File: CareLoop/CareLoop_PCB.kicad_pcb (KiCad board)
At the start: 2 copper layers, 38 parts, among them J1 Conn_01x02_Pin, J1_DEBUG1 Conn_01x04_Pin, J2 USB_B_Micro, J3 Conn_01x02_Pin, SW1 SW_Push, U1 nRF52840-QFXX, U2 MAX30102, U3 MPU-6050, U4 MCP1700x-330xxMB, U5 TP4056-42-ESOP8, Y1 32Mhz

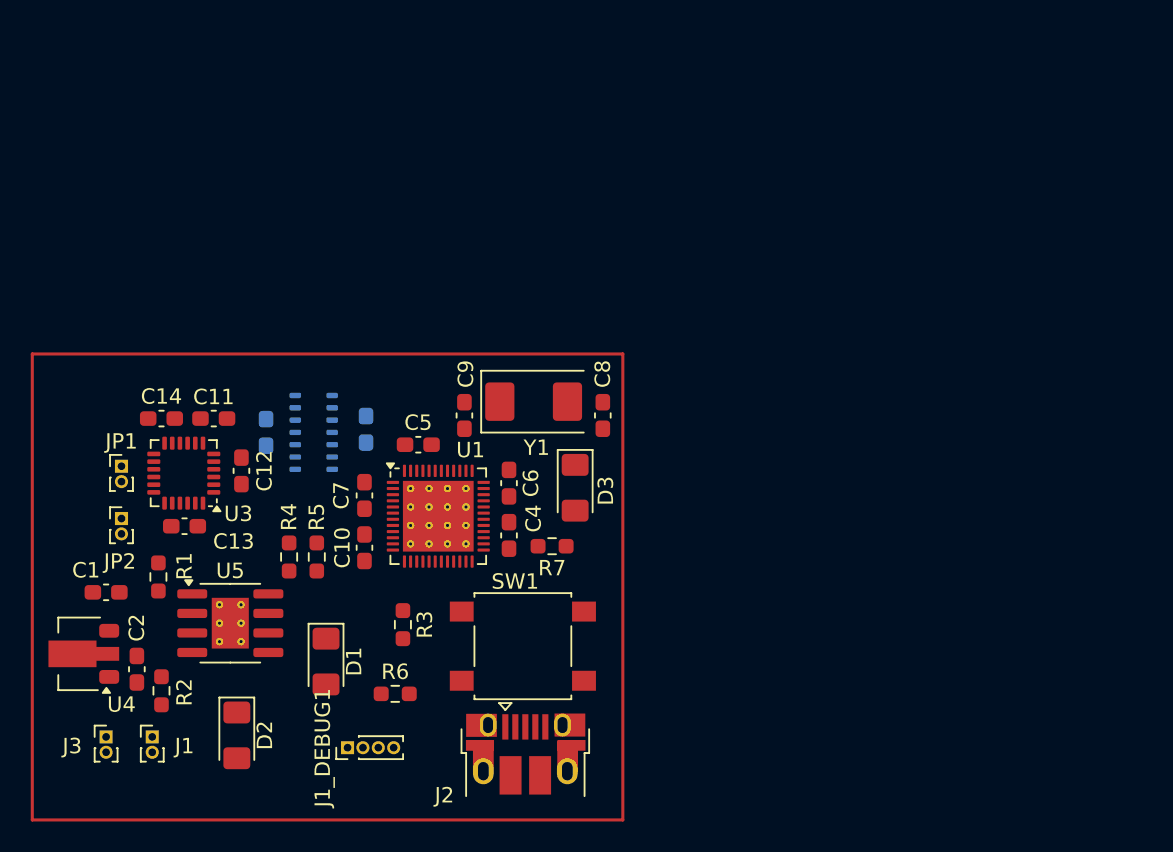
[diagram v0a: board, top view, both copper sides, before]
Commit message: WP: Placement PCB Parts done
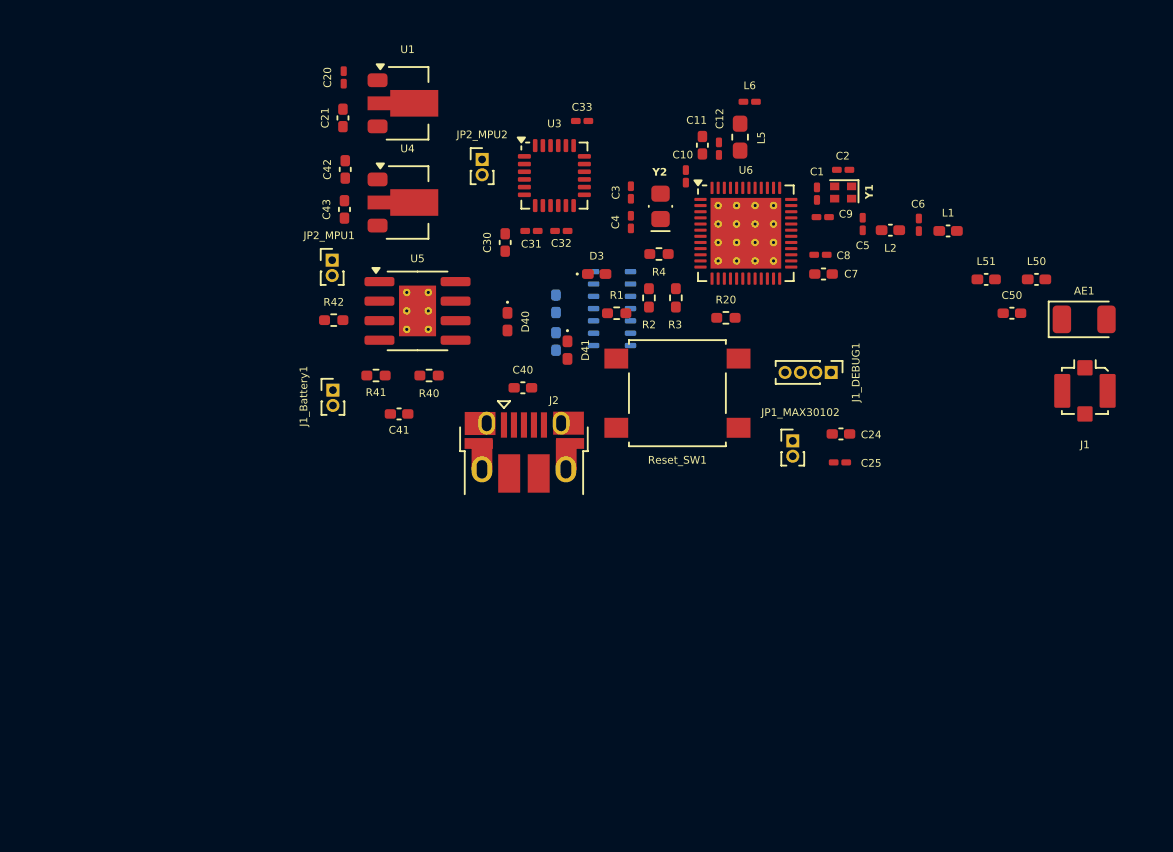
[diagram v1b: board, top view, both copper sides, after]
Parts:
- removed C13: 2.2n, Capacitor_SMD:C_0603_1608Metric_Pad1.08x0.95mm_HandSolder
- removed C14, C15: 100n, Capacitor_SMD:C_0603_1608Metric_Pad1.08x0.95mm_HandSolder
- removed D1, D2: LED, LED_SMD:LED_1206_3216Metric_Pad1.42x1.75mm_HandSolder
- removed J3: Conn_01x02_Pin, Connector_PinHeader_1.00mm:PinHeader_1x02_P1.00mm_Vertical
- removed JP1, JP2: Jumper_2_Bridged, Connector_PinHeader_1.00mm:PinHeader_1x02_P1.00mm_Vertical
- removed R5: 4k7, Resistor_SMD:R_0603_1608Metric_Pad0.98x0.95mm_HandSolder
- removed R6: 1k, Resistor_SMD:R_0603_1608Metric_Pad0.98x0.95mm_HandSolder
- removed R7: 325, Resistor_SMD:R_0603_1608Metric_Pad0.98x0.95mm_HandSolder
- removed SW1: SW_Push, Button_Switch_SMD:SW_SPST_B3S-1000
- added AE1: Antenna_Chip, RF_Antenna:Johanson_2450AT18x100, F.Cu at (192.8, 75.2)
- added C20: 100n, Capacitor_SMD:C_0201_0603Metric_Pad0.64x0.40mm_HandSolder, F.Cu at (144.7, 59.4)
- added C21: 4.7u, Capacitor_SMD:C_0402_1005Metric_Pad0.74x0.62mm_HandSolder, F.Cu at (144.6, 62.0)
- added C22: 1u, Capacitor_SMD:C_0402_1005Metric_Pad0.74x0.62mm_HandSolder, B.Cu at (158.5, 76.6)
- added C23: 4.7u, Capacitor_SMD:C_0402_1005Metric_Pad0.74x0.62mm_HandSolder, B.Cu at (158.5, 74.1)
- added C24: 10u, Capacitor_SMD:C_0402_1005Metric_Pad0.74x0.62mm_HandSolder, F.Cu at (177.0, 82.6)
- added C25: 100n, Capacitor_SMD:C_0201_0603Metric_Pad0.64x0.40mm_HandSolder, F.Cu at (176.9, 84.5)
- added C30: 10n, Capacitor_SMD:C_0402_1005Metric_Pad0.74x0.62mm_HandSolder, F.Cu at (155.2, 70.2)
- added C31: 100n, Capacitor_SMD:C_0201_0603Metric_Pad0.64x0.40mm_HandSolder, F.Cu at (156.9, 69.4)
- added C32: 100n, Capacitor_SMD:C_0201_0603Metric_Pad0.64x0.40mm_HandSolder, F.Cu at (158.8, 69.4)
- added C33: 2.2n, Capacitor_SMD:C_0201_0603Metric_Pad0.64x0.40mm_HandSolder, F.Cu at (160.2, 62.2)
- added C40: 1u, Capacitor_SMD:C_0402_1005Metric_Pad0.74x0.62mm_HandSolder, F.Cu at (156.3, 79.6)
- added C41: 10u, Capacitor_SMD:C_0402_1005Metric_Pad0.74x0.62mm_HandSolder, F.Cu at (148.2, 81.3)
- added C42: 1u, Capacitor_SMD:C_0402_1005Metric_Pad0.74x0.62mm_HandSolder, F.Cu at (144.8, 65.4)
- added C43: 1u, Capacitor_SMD:C_0402_1005Metric_Pad0.74x0.62mm_HandSolder, F.Cu at (144.7, 68.0)
- added C50: C_Small, Capacitor_SMD:C_0402_1005Metric_Pad0.74x0.62mm_HandSolder, F.Cu at (188.1, 74.8)
- added D40: LED, LED_SMD:LED_0402_1005Metric_Pad0.77x0.64mm_HandSolder, F.Cu at (155.3, 75.3)
- added D41: LED, LED_SMD:LED_0402_1005Metric_Pad0.77x0.64mm_HandSolder, F.Cu at (159.2, 77.2)
- added J1_Battery1: Conn_01x02_Pin, Connector_PinHeader_1.00mm:PinHeader_1x02_P1.00mm_Vertical, F.Cu at (143.9, 79.8)
- added JP1_MAX30102: Jumper_2_Bridged, Connector_PinHeader_1.00mm:PinHeader_1x02_P1.00mm_Vertical, F.Cu at (173.8, 83.0)
- added JP2_MPU1: Jumper_2_Bridged, Connector_PinHeader_1.00mm:PinHeader_1x02_P1.00mm_Vertical, F.Cu at (143.9, 71.3)
- added JP2_MPU2: Jumper_2_Bridged, Connector_PinHeader_1.00mm:PinHeader_1x02_P1.00mm_Vertical, F.Cu at (153.7, 64.8)
- added L1: 2.2n, Inductor_SMD:L_0402_1005Metric_Pad0.77x0.64mm_HandSolder, F.Cu at (183.9, 69.4)
- added L2: 4.7n, Inductor_SMD:L_0402_1005Metric_Pad0.77x0.64mm_HandSolder, F.Cu at (180.2, 69.3)
- added L5: 10u, Inductor_SMD:L_0603_1608Metric_Pad1.05x0.95mm_HandSolder, F.Cu at (170.4, 63.3)
- added L50: L_Small, Inductor_SMD:L_0402_1005Metric_Pad0.77x0.64mm_HandSolder, F.Cu at (189.7, 72.5)
- added L51: L_Small, Inductor_SMD:L_0402_1005Metric_Pad0.77x0.64mm_HandSolder, F.Cu at (186.4, 72.5)
- added L6: 15n, Inductor_SMD:L_0201_0603Metric_Pad0.64x0.40mm_HandSolder, F.Cu at (171.1, 61.0)
- added R20: 10k, Resistor_SMD:R_0402_1005Metric_Pad0.72x0.64mm_HandSolder, F.Cu at (169.5, 75.0)
- added R40: 1k, Resistor_SMD:R_0402_1005Metric_Pad0.72x0.64mm_HandSolder, F.Cu at (150.2, 78.8)
- added R41: 1k, Resistor_SMD:R_0402_1005Metric_Pad0.72x0.64mm_HandSolder, F.Cu at (146.8, 78.8)
- added R42: 20k, Resistor_SMD:R_0402_1005Metric_Pad0.72x0.64mm_HandSolder, F.Cu at (144.0, 75.2)
- added Reset_SW1: SW_Push, Button_Switch_SMD:SW_SPST_B3S-1000, F.Cu at (166.3, 80.0)
- added U6: nRF52840-QFXX, Package_DFN_QFN:QFN-48-1EP_6x6mm_P0.4mm_EP4.6x4.6mm_ThermalVias, F.Cu at (170.8, 69.5)
- added Y2: 32.768kHz, Crystal:Crystal_SMD_MicroCrystal_CM9V-T1A-2Pin_1.6x1.0mm_HandSoldering, F.Cu at (165.2, 67.8)
- C1, C2: value 1u -> 12p; footprint Capacitor_SMD:C_0603_1608Metric_Pad1.08x0.95mm_HandSolder -> Capacitor_SMD:C_0201_0603Metric_Pad0.64x0.40mm_HandSolder
- C10: value 100n -> 100p; footprint Capacitor_SMD:C_0603_1608Metric_Pad1.08x0.95mm_HandSolder -> Capacitor_SMD:C_0201_0603Metric_Pad0.64x0.40mm_HandSolder
- C11: value 10n -> 1u; footprint Capacitor_SMD:C_0603_1608Metric_Pad1.08x0.95mm_HandSolder -> Capacitor_SMD:C_0402_1005Metric_Pad0.74x0.62mm_HandSolder
- C12: footprint Capacitor_SMD:C_0603_1608Metric_Pad1.08x0.95mm_HandSolder -> Capacitor_SMD:C_0201_0603Metric_Pad0.64x0.40mm_HandSolder
- C3: value 1u -> 12p; footprint Capacitor_SMD:C_0603_1608Metric_Pad1.08x0.95mm_HandSolder -> Capacitor_SMD:C_0201_0603Metric_Pad0.64x0.40mm_HandSolder; moved to F.Cu
- C4: value 4.7u -> 12p; footprint Capacitor_SMD:C_0603_1608Metric_Pad1.08x0.95mm_HandSolder -> Capacitor_SMD:C_0201_0603Metric_Pad0.64x0.40mm_HandSolder
- C5: value 1.0u -> 1p; footprint Capacitor_SMD:C_0603_1608Metric_Pad1.08x0.95mm_HandSolder -> Capacitor_SMD:C_0201_0603Metric_Pad0.64x0.40mm_HandSolder
- C6: value 1.0u -> 1.2p; footprint Capacitor_SMD:C_0603_1608Metric_Pad1.08x0.95mm_HandSolder -> Capacitor_SMD:C_0201_0603Metric_Pad0.64x0.40mm_HandSolder
- C7: value 1.0u -> 1u; footprint Capacitor_SMD:C_0603_1608Metric_Pad1.08x0.95mm_HandSolder -> Capacitor_SMD:C_0402_1005Metric_Pad0.74x0.62mm_HandSolder
- C8: value 12p -> 47n; footprint Capacitor_SMD:C_0603_1608Metric_Pad1.08x0.95mm_HandSolder -> Capacitor_SMD:C_0201_0603Metric_Pad0.64x0.40mm_HandSolder
- C9: value 12p -> 100p; footprint Capacitor_SMD:C_0603_1608Metric_Pad1.08x0.95mm_HandSolder -> Capacitor_SMD:C_0201_0603Metric_Pad0.64x0.40mm_HandSolder
- D3: value LED -> LED_Small; footprint LED_SMD:LED_1206_3216Metric_Pad1.42x1.75mm_HandSolder -> LED_SMD:LED_0402_1005Metric_Pad0.77x0.64mm_HandSolder
- J1: value Conn_01x02_Pin -> Conn_Coaxial_Small; footprint Connector_PinHeader_1.00mm:PinHeader_1x02_P1.00mm_Vertical -> Connector_Coaxial:U.FL_Molex_MCRF_73412-0110_Vertical
- R1: value 20k -> 10k; footprint Resistor_SMD:R_0603_1608Metric_Pad0.98x0.95mm_HandSolder -> Resistor_SMD:R_0402_1005Metric_Pad0.72x0.64mm_HandSolder
- R2: value 1k -> 4k7; footprint Resistor_SMD:R_0603_1608Metric_Pad0.98x0.95mm_HandSolder -> Resistor_SMD:R_0402_1005Metric_Pad0.72x0.64mm_HandSolder
- R3: value 10k -> 4k7; footprint Resistor_SMD:R_0603_1608Metric_Pad0.98x0.95mm_HandSolder -> Resistor_SMD:R_0402_1005Metric_Pad0.72x0.64mm_HandSolder
- R4: value 4k7 -> 300; footprint Resistor_SMD:R_0603_1608Metric_Pad0.98x0.95mm_HandSolder -> Resistor_SMD:R_0402_1005Metric_Pad0.72x0.64mm_HandSolder
- U1: value nRF52840-QFXX -> MCP1700x-180xxMB; footprint Package_DFN_QFN:QFN-48-1EP_6x6mm_P0.4mm_EP4.6x4.6mm_ThermalVias -> Package_TO_SOT_SMD:SOT-89-3
- Y1: value 32Mhz -> 32MHz; footprint Crystal:Crystal_SMD_0603-2Pin_6.0x3.5mm -> Oscillator:Oscillator_SMD_Abracon_ASCO-4Pin_1.6x1.2mm
- moved J1 64.7 mm to (192.8, 79.8)
- moved C2 56.2 mm to (177.1, 65.4), turned to 0 degrees
- moved C1 53.0 mm to (175.4, 67.0), turned to 90 degrees
- moved R2 40.7 mm to (164.5, 73.8)
- moved J1_DEBUG1 39.8 mm to (176.3, 78.6), turned to -90 degrees
- moved C12 37.5 mm to (169.1, 64.0), turned to -90 degrees
- moved C11 36.4 mm to (168.0, 63.8), turned to -90 degrees
- moved U4 36.3 mm to (148.8, 67.5), turned to 0 degrees
- moved R1 34.4 mm to (162.4, 74.8), turned to 0 degrees
- moved C7 33.1 mm to (175.8, 72.2), turned to 0 degrees
- moved C5 32.3 mm to (178.4, 69.0), turned to 90 degrees
- moved C10 31.9 mm to (166.9, 65.8), turned to -90 degrees
- moved C6 31.5 mm to (182.1, 69.0), turned to 90 degrees
- moved R4 31.1 mm to (165.2, 70.9), turned to 180 degrees
- moved U3 30.9 mm to (158.3, 65.8), turned to 0 degrees
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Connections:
- C1 pad 1: /Battery/Vout -> GND
- C1 pad 2: Net-(J1-Pin_1) -> Net-(U6-XC1)
- C10 pad 1: /Battery/Vout -> GND
- C10 pad 2: GND -> Net-(U6-DEC1)
- C11 pad 1: Net-(U3-VLOGIC) -> GND
- C11 pad 2: GND -> /Battery/VCC
- C12 pad 1: Net-(U3-VDD) -> GND
- C12 pad 2: GND -> /Battery/VCC
- C2 pad 1: Net-(U4-VI) -> GND
- C2 pad 2: Net-(J1-Pin_1) -> Net-(U6-XC2)
- C3 pad 1: Net-(JP1-A) -> Net-(U6-P0.00)
- C4 pad 1: Net-(U1-DEC6) -> Net-(U6-P0.01)
- C5 pad 1: Net-(U1-DEC4) -> Net-(U6-ANT)
- C6 pad 1: Net-(U1-DEC3) -> Net-(C6-Pad1)
- C7 pad 1: Net-(U1-DEC1) -> Net-(U6-DEC4)
- C8 pad 1: GND -> Net-(U6-DEC4)
- C8 pad 2: Net-(U1-XC1) -> GND
- C9 pad 2: Net-(U1-XC2) -> Net-(U6-DEC3)
- J1 pad 1: Net-(J1-Pin_1) -> /Antenna/ANT
- J1 pad 2: Net-(J1-Pin_2) -> Net-(J1-Ext)
- J1_DEBUG1 pad 4: /Battery/Vout -> /Battery/VCC
- R1 pad 1: Net-(U5-PROG) -> Net-(U6-~{RESET})
- R1 pad 2: GND -> /Battery/VCC
- R2 pad 1: Net-(D2-A) -> /Battery/VCC
- R2 pad 2: Net-(J2-VBUS) -> /MAX30102/SDA
- R3 pad 1: Net-(U1-~{RESET}) -> /Battery/VCC
- R3 pad 2: /Battery/Vout -> /MAX30102/SCL
- R4 pad 1: /Battery/Vout -> Net-(U6-P0.07)
- R4 pad 2: /MAX30102/SDA -> Net-(D3-A)
- U1 pad 1: Net-(U1-DEC1) -> GND
- U1 pad 2: /MCU/INT_MPU -> Net-(JP1_MAX30102-A)
- U1 pad 3: unconnected-(U1-P0.01-Pad3) -> Net-(U1-VO)
- U2 pad 10: Net-(JP1-A) -> Net-(JP1_MAX30102-A)
- U2 pad 11: Net-(JP1-A) -> Net-(U1-VO)
- U2 pad 13: unconnected-(U2-~{INT}-Pad13) -> /MAX30102/MAX_INT
- U2 pad 9: Net-(JP1-A) -> Net-(JP1_MAX30102-A)
- U3 pad 13: Net-(U3-VDD) -> Net-(JP2_MPU2-A)
- U3 pad 8: Net-(U3-VLOGIC) -> Net-(JP2_MPU2-A)
- U4 pad 1: Net-(J1-Pin_1) -> GND
- U4 pad 2: Net-(U4-VI) -> Net-(JP2_MPU1-A)
- U4 pad 3: /Battery/Vout -> /Battery/VCC
- U5 pad 5: Net-(J1-Pin_2) -> Net-(J1_Battery1-Pin_2)
- U5 pad 8: GND -> Net-(J2-VBUS)
- Y1 pad 1: Net-(U1-XC2) -> Net-(U6-XC2)
- Y1 pad 2: Net-(U1-XC1) -> (no net)

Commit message: WP: updatet version with routing
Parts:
- added C26: 100p, Capacitor_SMD:C_0201_0603Metric_Pad0.64x0.40mm_HandSolder, F.Cu at (155.7, 71.8)
- added C27: 100n, Capacitor_SMD:C_0201_0603Metric_Pad0.64x0.40mm_HandSolder, F.Cu at (155.7, 70.1)
- added R21: 200k, Resistor_SMD:R_0402_1005Metric_Pad0.72x0.64mm_HandSolder, F.Cu at (159.4, 68.8)
- added R22: 4k7, Resistor_SMD:R_0402_1005Metric_Pad0.72x0.64mm_HandSolder, F.Cu at (157.5, 74.0)
- added R23: 4k7, Resistor_SMD:R_0402_1005Metric_Pad0.72x0.64mm_HandSolder, F.Cu at (158.8, 74.1)
- added U7: PCA9306, Package_SON:X2SON-8_1.4x1mm_P0.35mm, F.Cu at (158.2, 71.0)
- U6: footprint Package_DFN_QFN:QFN-48-1EP_6x6mm_P0.4mm_EP4.6x4.6mm_ThermalVias -> Package_DFN_QFN:QFN-48-1EP_6x6mm_P0.4mm_EP4.6x4.6mm
- moved R41 13.7 mm to (160.4, 79.5), turned to -90 degrees
- moved C30 12.1 mm to (155.3, 58.0), turned to -90 degrees
- moved C31 11.7 mm to (156.7, 57.7), turned to -90 degrees
- moved C32 11.5 mm to (159.8, 57.9)
- moved C7 8.38 mm to (181.7, 66.2)
- moved R40 7.53 mm to (157.6, 77.2), turned to -90 degrees
- moved C40 7.14 mm to (149.3, 78.2)
- moved JP2_MPU2 4.37 mm to (154.1, 60.4)
- moved U3 4.37 mm to (158.8, 61.5), turned to 180 degrees
- moved C8 3.34 mm to (176.4, 67.7)
- moved C33 3.30 mm to (158.4, 65.0)
- moved J1_DEBUG1 2.19 mm to (174.4, 77.6), turned to 90 degrees
- moved R2 2.05 mm to (166.6, 73.7)
- moved C9 1.90 mm to (176.4, 66.7)
- moved D40 1.85 mm to (155.2, 77.2)
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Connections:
- U2 pad 2: /MAX30102/SCL -> Net-(U2-SCL)
- U2 pad 3: /MAX30102/SDA -> Net-(U2-SDA)
- U6 pad 22: /MCU/INT_MPU -> unconnected-(U6-P0.23-Pad22)
- U6 pad 4: unconnected-(U6-P0.04-Pad4) -> /MCU/INT_MPU
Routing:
- net /Battery/VCC: track 0.00 -> 89.6 mm, vias 0 -> 4
- net Net-(JP1_MAX30102-A): track 0.00 -> 53.6 mm, vias 0 -> 1
- net /MAX30102/SDA: track 0.00 -> 34.4 mm
- net Net-(U6-DEC4): track 0.00 -> 29.2 mm
- net Net-(U1-VO): track 0.00 -> 29.0 mm, vias 0 -> 1
- net /MAX30102/MAX_INT: track 0.00 -> 26.5 mm, vias 0 -> 1
- net /MAX30102/SCL: track 0.00 -> 26.4 mm, vias 0 -> 2
- net /MCU/INT_MPU: track 0.00 -> 25.2 mm
- net Net-(J1_Battery1-Pin_2): track 0.00 -> 21.3 mm
- net Net-(U2-SCL): track 0.00 -> 19.3 mm, vias 0 -> 1
- net Net-(U2-SDA): track 0.00 -> 13.2 mm, vias 0 -> 1
- net Net-(J2-VBUS): track 0.00 -> 12.6 mm
- net Net-(JP2_MPU1-A): track 0.00 -> 11.2 mm
- net Net-(U6-~{RESET}): track 0.00 -> 9.00 mm
- net Net-(D41-K): track 0.00 -> 8.70 mm
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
